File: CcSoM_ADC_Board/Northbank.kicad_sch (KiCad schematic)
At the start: 1 part, among them J1 SoM Connector

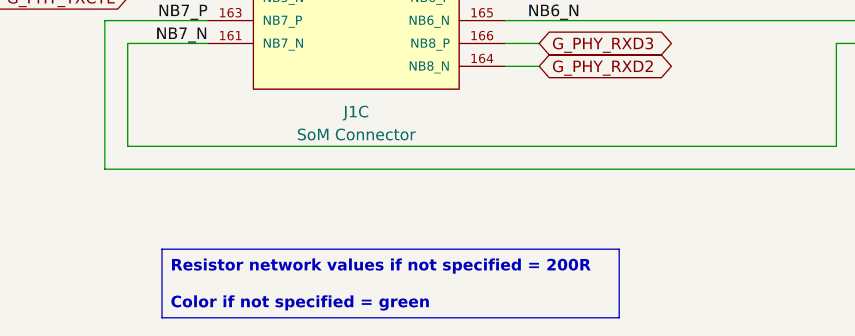
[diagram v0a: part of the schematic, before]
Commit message: corrected schematic created pdf and bom file
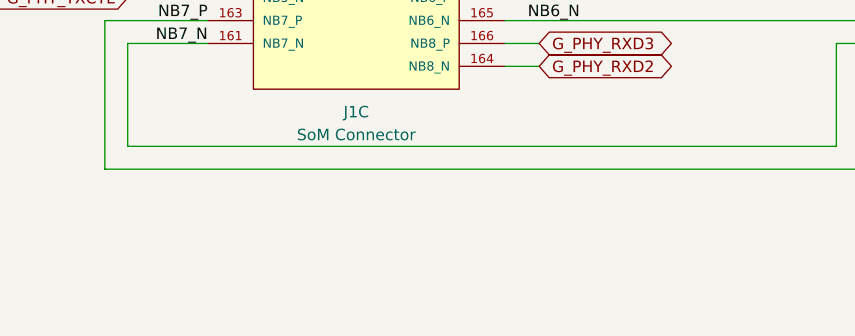
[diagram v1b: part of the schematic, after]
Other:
- title: SoM Programmer & Tester -> SoM Programmer & ADC Board
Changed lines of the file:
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@@
 	(paper "A4")
 	(title_block
-		(title "SoM Programmer & Tester")
-		(date "2024-12-20")
+		(title "SoM Programmer & ADC Board")
+		(date "2026-02-09")
 		(rev "0.1")
 		(company "Technische Hochschule Köln")
 		(comment 1 "Felix Sebastian Nitz")
+		(comment 2 "Ismail Özdemirkan")
 	)
 	(bus_alias "East_A"
@@
 		)
 	)
-	(text_box "Resistor network values if not specified = 200R\n\nColor if not specified = green"
-		(exclude_from_sim no)
-		(at 116.84 140.97 0)
-		(size 50.8 7.62)
-		(margins 0.9525 0.9525 0.9525 0.9525)
-		(stroke
-			(width 0)
-			(type default)
-		)
-		(fill
-			(type none)
-		)
-		(effects
-			(font
-				(size 1.27 1.27)
-				(thickness 0.254)
-				(bold yes)
-			)
-			(justify left)
-		)
-	)

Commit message: digikey no not complete
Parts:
- J1: DigiKey_no (none) -> A121565-ND
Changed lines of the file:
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@@
+			)
+		)
+		(property "DigiKey_no" "A121565-ND"
+			(at 138.43 86.36 0)
+			(effects
+				(font
+					(size 1.27 1.27)
+				)
+				(hide yes)
 			)
 		)
